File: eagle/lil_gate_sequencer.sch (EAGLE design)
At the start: 63 parts, among them IC3 4017N, IC4 4093N, Q1 2N3904, Q2 2N3904

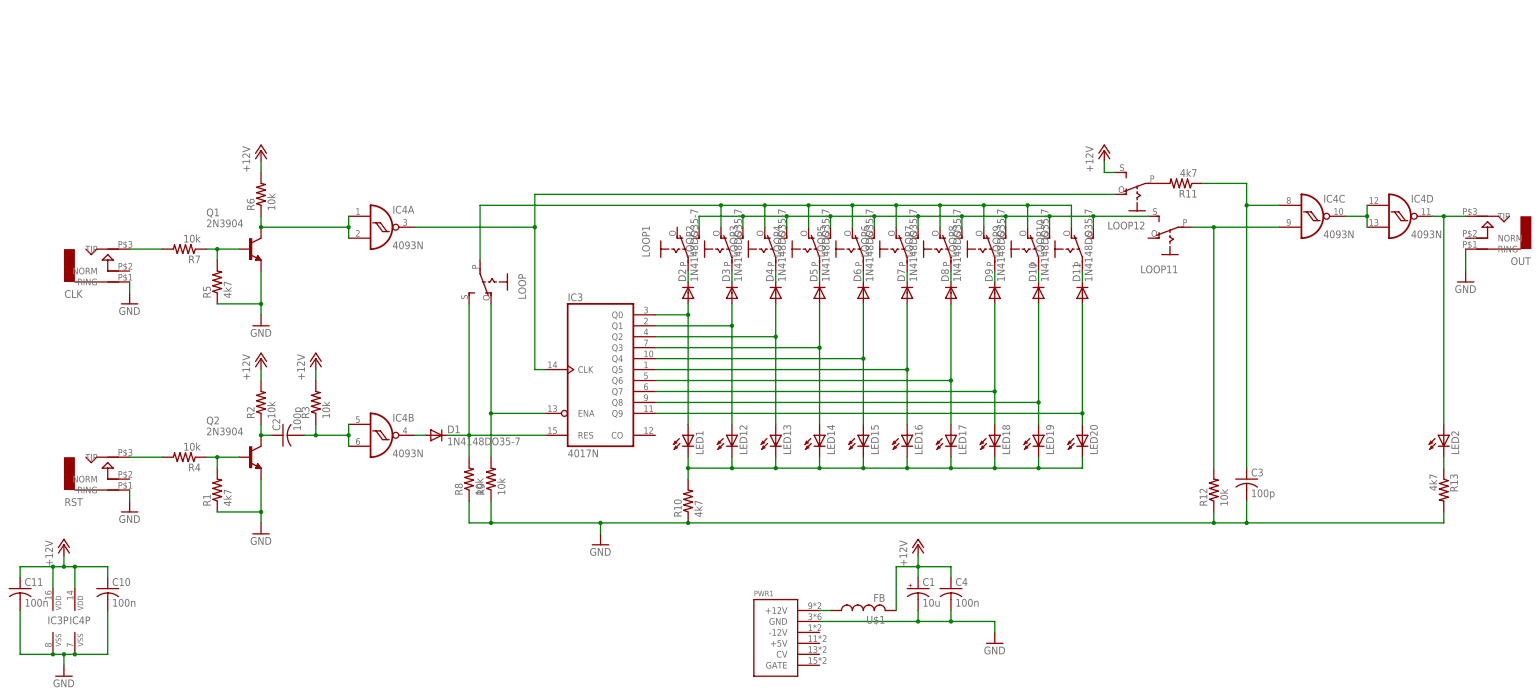
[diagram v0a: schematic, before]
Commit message: renumbered parts
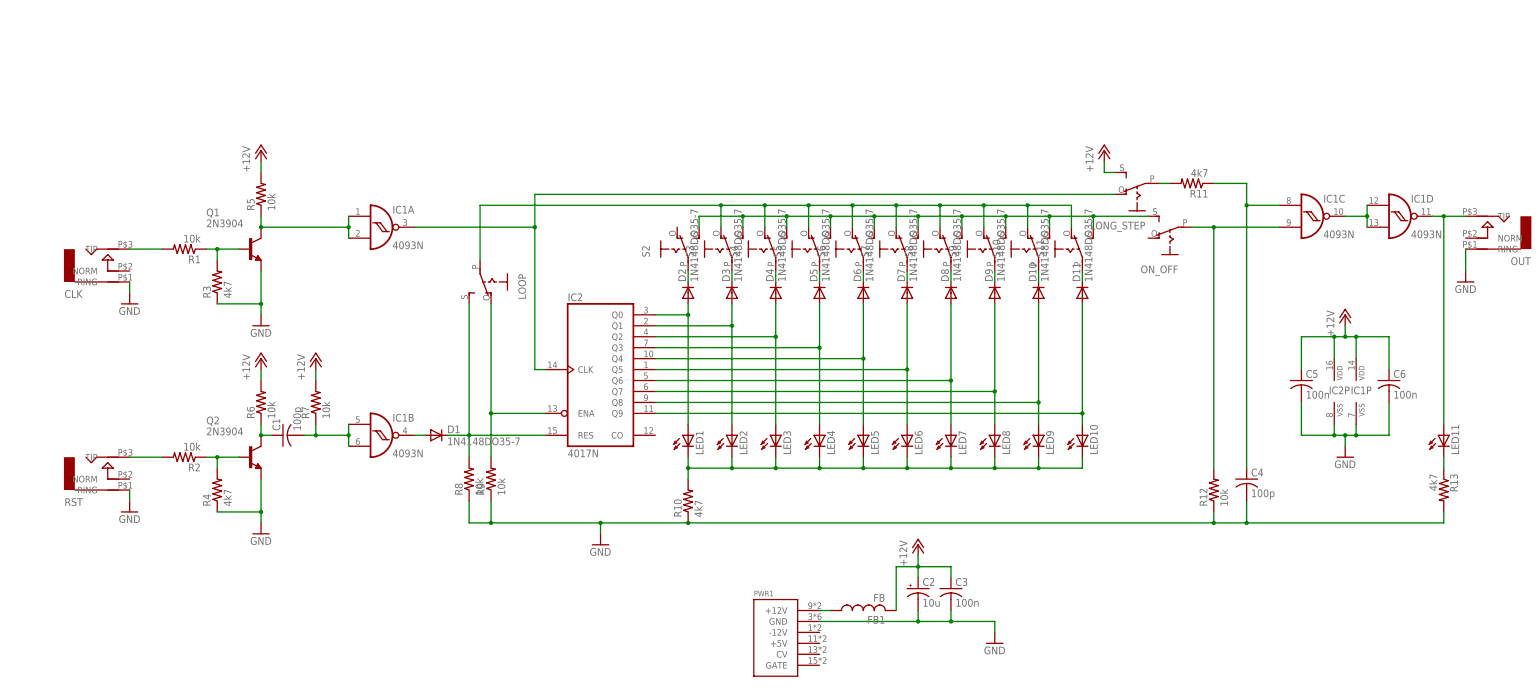
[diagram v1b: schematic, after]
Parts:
- removed C10, C11: 100n, rcl:C-US050-024X044
- removed LED12: (no value), led:LED5MM
- added C5, C6: 100n, rcl:C-US050-024X044
- added LED11: (no value), led:LED5MM
- C1: value 10u -> 100p; device rcl:CPOL-USB45181A -> rcl:C-US050-024X044
- C2: value 100p -> 10u; device rcl:C-US050-024X044 -> rcl:CPOL-USB45181A
- C3: value 100p -> 100n
- C4: value 100n -> 100p
- R1, R5: value 4k7 -> 10k
- R3, R4: value 10k -> 4k7
- renumbered IC3 to IC2, IC4 to IC1, LED13 to LED3, LED14 to LED4, LED15 to LED5, LED16 to LED6, LED17 to LED7, LED18 to LED8, LED19 to LED9, LED20 to LED10, LOOP1 to S2, LOOP10 to S11, LOOP11 to ON_OFF, LOOP12 to LONG_STEP, LOOP2 to S3, LOOP3 to S4, LOOP4 to S5, LOOP5 to S6, LOOP6 to S7, LOOP7 to S8, LOOP8 to S9, LOOP9 to S10, U$1 to FB1
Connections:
- net +12V: now also C2.+, C3.1, C5.1, C6.1, R5.2, R7.2; no longer C1.+, C10.1, C11.1, C4.1, R2.2, R3.2
- net GND: now also C2.-, C5.2, C6.2, R3.1, R4.1; no longer C1.-, C10.2, C11.2, R1.1, R5.1
- net N$10: now also C1.2, R7.1; no longer C2.2, R3.1
- net N$11: now also C1.1, R6.1; no longer C2.1, R2.1
- net N$17: now also LED2.A; no longer LED12.A
- net N$2: now also R2.1, R4.2; no longer R1.2, R4.1
- net N$35: now also LED2.C; no longer LED12.C
- net N$4: now also R1.1, R3.2; no longer R5.2, R7.1
- net N$41: now also C4.1; no longer C3.1
- net N$43: now also LED11.C; no longer LED2.C
- net N$5: now also R5.1; no longer R6.1
- net N$6: now also LED11.A; no longer LED2.A
- net N$7: now also R1.2; no longer R7.2
- net N$8: now also R2.2; no longer R4.2
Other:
- moved on the sheet: C3, C4, LED2, R1, R11, R2, R3, R4, R5, R6, R7

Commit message: jameco toggle part
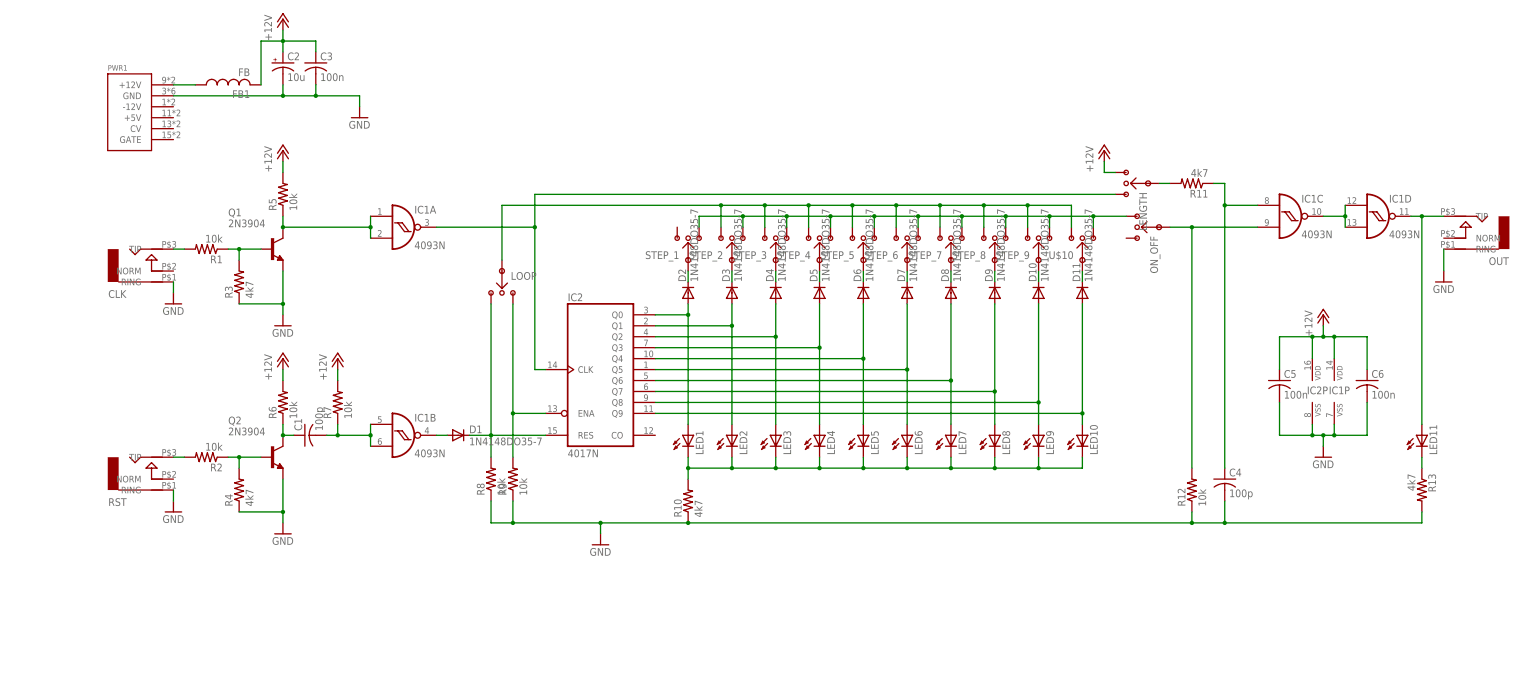
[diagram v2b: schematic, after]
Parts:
- removed LONG_STEP, S10, S11, S2, S3, S4, S5, S6, S7, S8, S9: (no value), adafruit:EG1218S
- added LENGTH, STEP_1, STEP_2, STEP_3, STEP_4, STEP_5, STEP_6, STEP_7, STEP_8, STEP_9, U$10: MTS-102-C4, jameco:MTS-102-C4
- LOOP, ON_OFF: value (none) -> MTS-102-C4; device adafruit:EG1218S -> jameco:MTS-102-C4
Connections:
- net +12V: now also LENGTH.P$1; no longer LONG_STEP.S
- net N$12: now also LENGTH.P$2; no longer LONG_STEP.O
- net N$13: now also STEP_1.P$3; no longer S2.P
- net N$14: now also LOOP.P$2; no longer LOOP.O
- net N$16: now also STEP_2.P$3; no longer S3.P
- net N$18: now also STEP_3.P$3; no longer S4.P
- net N$20: now also STEP_4.P$3; no longer S5.P
- net N$22: now also STEP_5.P$3; no longer S6.P
- net N$24: now also STEP_6.P$3; no longer S7.P
- net N$26: now also STEP_7.P$3; no longer S8.P
- net N$28: now also STEP_8.P$3; no longer S9.P
- net N$30: now also STEP_9.P$3; no longer S10.P
- net N$32: now also U$10.P$3; no longer S11.P
- net N$34: now also LOOP.P$3, STEP_2.P$2, STEP_3.P$2, STEP_4.P$2, STEP_5.P$2, STEP_6.P$2, STEP_7.P$2, STEP_8.P$2, STEP_9.P$2, U$10.P$2; no longer LOOP.P, S10.O, S11.O, S3.O, S4.O, S5.O, S6.O, S7.O, S8.O, S9.O
- net N$36: now also ON_OFF.P$1, STEP_1.P$1, STEP_2.P$1, STEP_3.P$1, STEP_4.P$1, STEP_5.P$1, STEP_6.P$1, STEP_7.P$1, STEP_8.P$1, STEP_9.P$1, U$10.P$1; no longer ON_OFF.S, S10.S, S11.S, S2.S, S3.S, S4.S, S5.S, S6.S, S7.S, S8.S, S9.S
- net N$37: now also LENGTH.P$3; no longer LONG_STEP.P
- net N$38: now also ON_OFF.P$3; no longer ON_OFF.P
- net N$6: now also IC1D.O
- net N$9: now also LOOP.P$1; no longer LOOP.S
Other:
- moved on the sheet: C1, C2, C3, C4, C5, C6, CLK, D1, FB1, IC1A, IC1B, IC1C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

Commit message: layout begins
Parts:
- removed LENGTH, ON_OFF: MTS-102-C4, jameco:MTS-102-C4
- added ENABLE_1, ENABLE_2, LENGTH_1, LENGTH_LONG, LENGTH_SHORT, LOOP_1, LOOP_ON: LSP11, solpad:LSP11
- D1: value 1N4148DO35-7 -> 1N4148DO35-10; device diode:1N4148DO35-7 -> diode:1N4148DO35-10
- LOOP: value MTS-102-C4 -> LSP11; device jameco:MTS-102-C4 -> solpad:LSP11
- R10: device rcl:R-US_0207/7 -> rcl:R-US_0309/12
- renumbered U$10 to STEP_10
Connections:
- net +12V: now also LENGTH_LONG.MP; no longer LENGTH.P$1
- net GND: now also CLK.NORM
- net N$12: now also LENGTH_SHORT.MP; no longer LENGTH.P$2
- net N$14: now also LOOP_1.MP; no longer LOOP.P$2
- net N$34: now also LOOP.MP; no longer LOOP.P$3
- net N$36: now also ENABLE_1.MP; no longer ON_OFF.P$1
- net N$37: now also LENGTH_1.MP; no longer LENGTH.P$3
- net N$38: now also ENABLE_2.MP; no longer ON_OFF.P$3
- net N$9: now also LOOP_ON.MP; no longer LOOP.P$1
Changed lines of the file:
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@@
 <part name="P+1" library="supply1" deviceset="+12V" device=""/>
 <part name="P+3" library="supply1" deviceset="+12V" device=""/>
-<part name="D1" library="diode" deviceset="1N4148" device="DO35-7"/>
+<part name="D1" library="diode" deviceset="1N4148" device="DO35-10" value="1N4148DO35-10"/>
 <part name="C1" library="rcl" deviceset="C-US" device="050-024X044" value="100p"/>
 <part name="R8" library="rcl" deviceset="R-US_" device="0207/7" value="10k"/>
@@
 <part name="LED10" library="led" deviceset="LED" device="5MM"/>
 <part name="D11" library="diode" deviceset="1N4148" device="DO35-7"/>
-<part name="R10" library="rcl" deviceset="R-US_" device="0207/7" value="4k7"/>
+<part name="R10" library="rcl" deviceset="R-US_" device="0309/12" value="4k7"/>
 <part name="P+5" library="supply1" deviceset="+12V" device=""/>
 <part name="R11" library="rcl" deviceset="R-US_" device="0207/7" value="4k7"/>
@@
 <part name="LED11" library="led" deviceset="LED" device="5MM"/>
 <part name="R13" library="rcl" deviceset="R-US_" device="0207/7" value="4k7"/>
-<part name="LOOP" library="jameco" deviceset="MTS-102-C4" device=""/>
 <part name="STEP_1" library="jameco" deviceset="MTS-102-C4" device=""/>
 <part name="STEP_2" library="jameco" deviceset="MTS-102-C4" device=""/>
@@
 <part name="STEP_8" library="jameco" deviceset="MTS-102-C4" device=""/>
 <part name="STEP_9" library="jameco" deviceset="MTS-102-C4" device=""/>
-<part name="U$10" library="jameco" deviceset="MTS-102-C4" device=""/>
-<part name="LENGTH" library="jameco" deviceset="MTS-102-C4" device=""/>
-<part name="ON_OFF" library="jameco" deviceset="MTS-102-C4" device=""/>
+<part name="STEP_10" library="jameco" deviceset="MTS-102-C4" device=""/>
+<part name="LOOP_ON" library="solpad" deviceset="LSP11" device=""/>
+<part name="LOOP_1" library="solpad" deviceset="LSP11" device=""/>
+<part name="LOOP" library="solpad" deviceset="LSP11" device=""/>
+<part name="ENABLE_1" library="solpad" deviceset="LSP11" device=""/>
+<part name="ENABLE_2" library="solpad" deviceset="LSP11" device=""/>
+<part name="LENGTH_1" library="solpad" deviceset="LSP11" device=""/>
+<part name="LENGTH_LONG" library="solpad" deviceset="LSP11" device=""/>
+<part name="LENGTH_SHORT" library="solpad" deviceset="LSP11" device=""/>
 </parts>
 <sheets>
@@
 <instance part="LED11" gate="G$1" x="312.42" y="55.88"/>
 <instance part="R13" gate="G$1" x="312.42" y="43.18" rot="R270"/>
-<instance part="LOOP" gate="G$1" x="99.06" y="88.9" rot="R270"/>
 <instance part="STEP_1" gate="G$1" x="142.24" y="101.6" rot="R90"/>
 <instance part="STEP_2" gate="G$1" x="152.4" y="101.6" rot="R90"/>
@@
 <instance part="STEP_8" gate="G$1" x="213.36" y="101.6" rot="R90"/>
 <instance part="STEP_9" gate="G$1" x="223.52" y="101.6" rot="R90"/>
-<instance part="U$10" gate="G$1" x="233.68" y="101.6" rot="R90"/>
-<instance part="LENGTH" gate="G$1" x="243.84" y="114.3" rot="R180"/>
-<instance part="ON_OFF" gate="G$1" x="246.38" y="104.14" rot="R180"/>
+<instance part="STEP_10" gate="G$1" x="233.68" y="101.6" rot="R90"/>
+<instance part="LOOP_ON" gate="1" x="96.52" y="88.9"/>
+<instance part="LOOP_1" gate="1" x="101.6" y="88.9"/>
+<instance part="LOOP" gate="1" x="99.06" y="93.98" rot="R180"/>
+<instance part="ENABLE_1" gate="1" x="246.38" y="106.68" rot="R270"/>
+<instance part="ENABLE_2" gate="1" x="251.46" y="104.14" rot="R90"/>
+<instance part="LENGTH_1" gate="1" x="248.92" y="114.3" rot="R90"/>
+<instance part="LENGTH_LONG" gate="1" x="243.84" y="116.84" rot="R270"/>
+<instance part="LENGTH_SHORT" gate="1" x="243.84" y="111.76" rot="R270"/>
 </instances>
 <busses>
@@
 <wire x1="238.76" y1="119.38" x2="238.76" y2="116.84" width="0.1524" layer="91"/>
 <wire x1="238.76" y1="116.84" x2="241.3" y2="116.84" width="0.1524" layer="91"/>
-<pinref part="LENGTH" gate="G$1" pin="P$1"/>
+<pinref part="LENGTH_LONG" gate="1" pin="MP"/>
 </segment>
 </net>
@@
 <pinref part="GND1" gate="1" pin="GND"/>
 <wire x1="22.86" y1="88.9" x2="22.86" y2="91.44" width="0.1524" layer="91"/>
+<pinref part="CLK" gate="G$1" pin="NORM"/>
+<wire x1="22.86" y1="93.98" x2="22.86" y2="91.44" width="0.1524" layer="91"/>
+<junction x="22.86" y="91.44"/>
 </segment>
 <segment>
@@
 <junction x="96.52" y="55.88"/>
 <wire x1="96.52" y1="55.88" x2="96.52" y2="50.8" width="0.1524" layer="91"/>
-<pinref part="LOOP" gate="G$1" pin="P$1"/>
+<pinref part="LOOP_ON" gate="1" pin="MP"/>
 </segment>
 </net>
@@
 <wire x1="106.68" y1="111.76" x2="106.68" y2="104.14" width="0.1524" layer="91"/>
 <junction x="106.68" y="104.14"/>
-<pinref part="LENGTH" gate="G$1" pin="P$2"/>
+<pinref part="LENGTH_SHORT" gate="1" pin="MP"/>
 </segment>
 </net>
@@
 <wire x1="109.22" y1="60.96" x2="101.6" y2="60.96" width="0.1524" layer="91"/>
 <junction x="101.6" y="60.96"/>
-<pinref part="LOOP" gate="G$1" pin="P$2"/>
+<pinref part="LOOP_1" gate="1" pin="MP"/>
 </segment>
 </net>
@@
 <pinref part="D11" gate="G$1" pin="C"/>
 <wire x1="233.68" y1="93.98" x2="233.68" y2="91.44" width="0.1524" layer="91"/>
-<pinref part="U$10" gate="G$1" pin="P$3"/>
+<pinref part="STEP_10" gate="G$1" pin="P$3"/>
 </segment>
 </net>
@@
 <wire x1="231.14" y1="109.22" x2="231.14" y2="104.14" width="0.1524" layer="91"/>
 <junction x="220.98" y="109.22"/>
-<pinref part="LOOP" gate="G$1" pin="P$3"/>
 <pinref part="STEP_2" gate="G$1" pin="P$2"/>
 <pinref part="STEP_3" gate="G$1" pin="P$2"/>
@@
 <pinref part="STEP_8" gate="G$1" pin="P$2"/>
 <pinref part="STEP_9" gate="G$1" pin="P$2"/>
-<pinref part="U$10" gate="G$1" pin="P$2"/>
+<pinref part="STEP_10" gate="G$1" pin="P$2"/>
+<pinref part="LOOP" gate="1" pin="MP"/>
 </segment>
 </net>
@@
 <pinref part="STEP_8" gate="G$1" pin="P$1"/>
 <pinref part="STEP_9" gate="G$1" pin="P$1"/>
-<pinref part="U$10" gate="G$1" pin="P$1"/>
-<pinref part="ON_OFF" gate="G$1" pin="P$1"/>
+<pinref part="STEP_10" gate="G$1" pin="P$1"/>
+<pinref part="ENABLE_1" gate="1" pin="MP"/>
 </segment>
 </net>
@@
 <pinref part="R11" gate="G$1" pin="2"/>
 <wire x1="254" y1="114.3" x2="251.46" y2="114.3" width="0.1524" layer="91"/>
-<pinref part="LENGTH" gate="G$1" pin="P$3"/>
+<pinref part="LENGTH_1" gate="1" pin="MP"/>
 </segment>
 </net>
@@
 <wire x1="259.08" y1="104.14" x2="274.32" y2="104.14" width="0.1524" layer="91"/>
 <junction x="259.08" y="104.14"/>
-<pinref part="ON_OFF" gate="G$1" pin="P$3"/>
-</segment>
-</net>
+<pinref part="ENABLE_2" gate="1" pin="MP"/>
+</segment>
+</net>

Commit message: more routes
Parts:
- R10: device rcl:R-US_0309/12 -> rcl:R-US_0207/7
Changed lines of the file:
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@@
 <part name="LED10" library="led" deviceset="LED" device="5MM"/>
 <part name="D11" library="diode" deviceset="1N4148" device="DO35-7"/>
-<part name="R10" library="rcl" deviceset="R-US_" device="0309/12" value="4k7"/>
+<part name="R10" library="rcl" deviceset="R-US_" device="0207/7" value="4k7"/>
 <part name="P+5" library="supply1" deviceset="+12V" device=""/>
 <part name="R11" library="rcl" deviceset="R-US_" device="0207/7" value="4k7"/>
